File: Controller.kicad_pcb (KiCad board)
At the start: 2 copper layers, 43.3 x 67.5 mm, 24 parts, among them IC1 SN74HCT245PWR, IC2 SN74HCT245PWR, J1 RGB_3_pin, J10 RGB_3_pin, J11 AMP_Mate-N-Lok_Power, J2 RGB_3_pin, J3 RGB_3_pin, J4 RGB_3_pin, J5 RGB_3_pin, J6 RGB_3_pin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

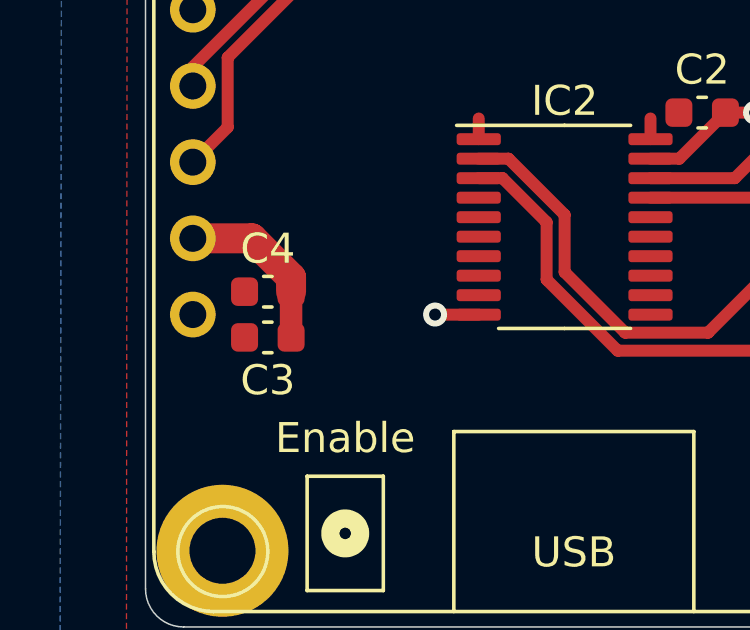
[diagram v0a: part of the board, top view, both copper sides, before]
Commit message: Use 47uF capacitor which is available in JLC's basic library.
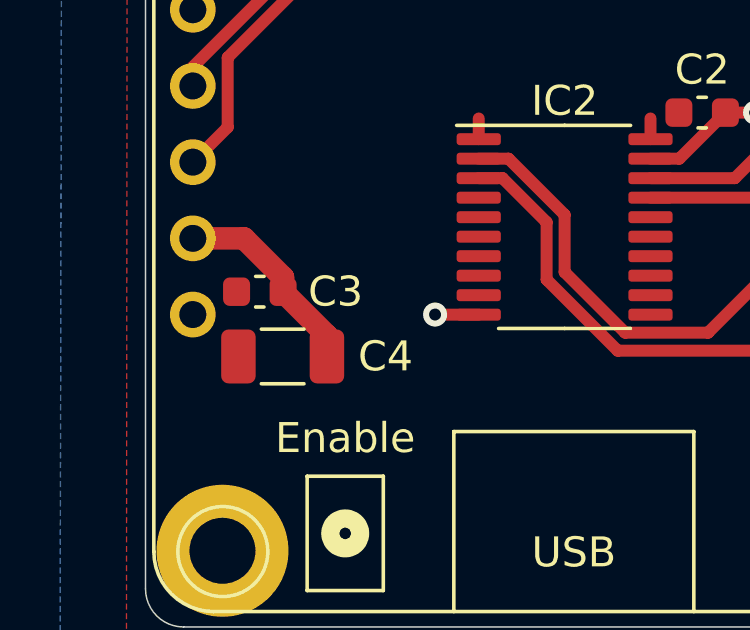
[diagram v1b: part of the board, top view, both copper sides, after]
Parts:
- C4: footprint Capacitor_SMD:C_0603_1608Metric -> Capacitor_SMD:C_1206_3216Metric
- moved C4 2.22 mm to (148.1, 137.3)
- moved C3 1.55 mm to (147.3, 135.1)
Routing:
- net GND: track 17.1 -> 18.1 mm
